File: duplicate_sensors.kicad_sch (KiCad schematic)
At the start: 0 parts

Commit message: IR + DC mic
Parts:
- added C1: 10nF, symbol Device:C
- added J1: SENO232_MIC, Connector_Audio:Jack_XLR_Neutrik_NC3FAAH_Horizontal, symbol Connector_Generic:Conn_01x03
- added Q1: AO3400A, Package_TO_SOT_SMD:SOT-23, symbol Transistor_FET:AO3400A
- added R1: 1k, symbol Device:R
- added R2: 39, Package_DIP:DIP-8_W7.62mm, symbol Device:R
- added R3: 100, Package_DIP:DIP-8_W7.62mm, symbol Device:R
- added R4: 100k, Package_DIP:DIP-8_W7.62mm, symbol Device:R
- added TSAL6200: LED, Package_DirectFET:DirectFET_MD, symbol Device:LED
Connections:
- new net: Q1.1 (G), R3.1, R4.1
- new net: J1.1 (Pin_1), R1.1
- new net: C1.1, R1.2
- new net: R2.2, TSAL6200.2 (A)
- new net: Q1.3 (D), TSAL6200.1 (K)
- new net +3.3V: J1.2 (Pin_2), R2.1
- new net GND: C1.2, J1.3 (Pin_3), Q1.2 (S), R4.2

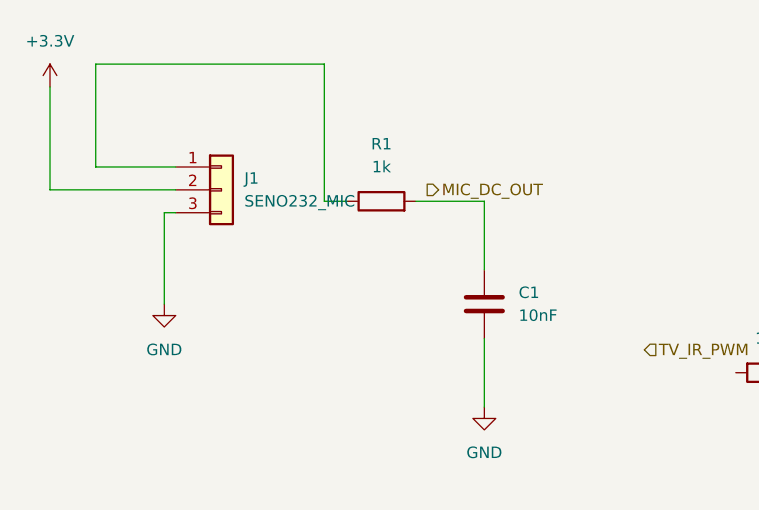
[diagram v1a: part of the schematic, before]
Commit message: Update duplicate_sensors.kicad_sch
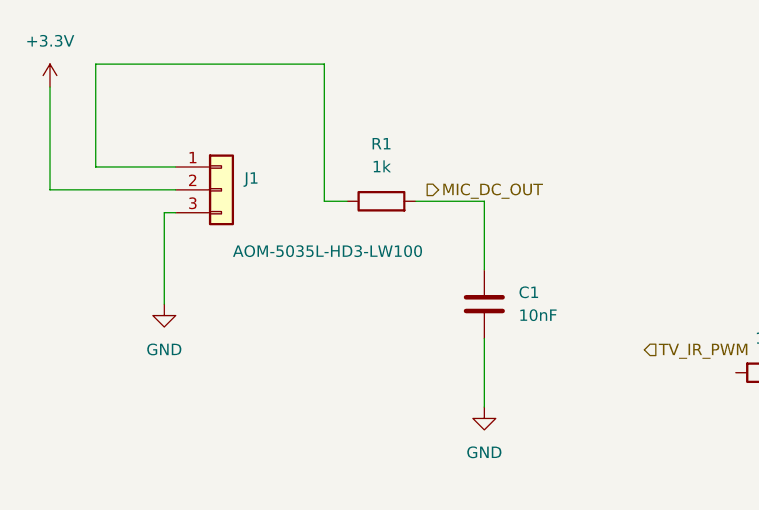
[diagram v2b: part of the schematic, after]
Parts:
- J1: value SENO232_MIC -> AOM-5035L-HD3-LW100
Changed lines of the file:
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@@
 		(in_pos_files yes)
 		(dnp no)
-		(fields_autoplaced yes)
 		(property "Reference" "J1"
 			(at 64.77 46.9899 0)
@@
 			)
 		)
-		(property "Value" "SENO232_MIC"
-			(at 64.77 49.5299 0)
+		(property "Value" "AOM-5035L-HD3-LW100"
+			(at 63.5 55.118 0)
 			(show_name no)
 			(do_not_autoplace no)

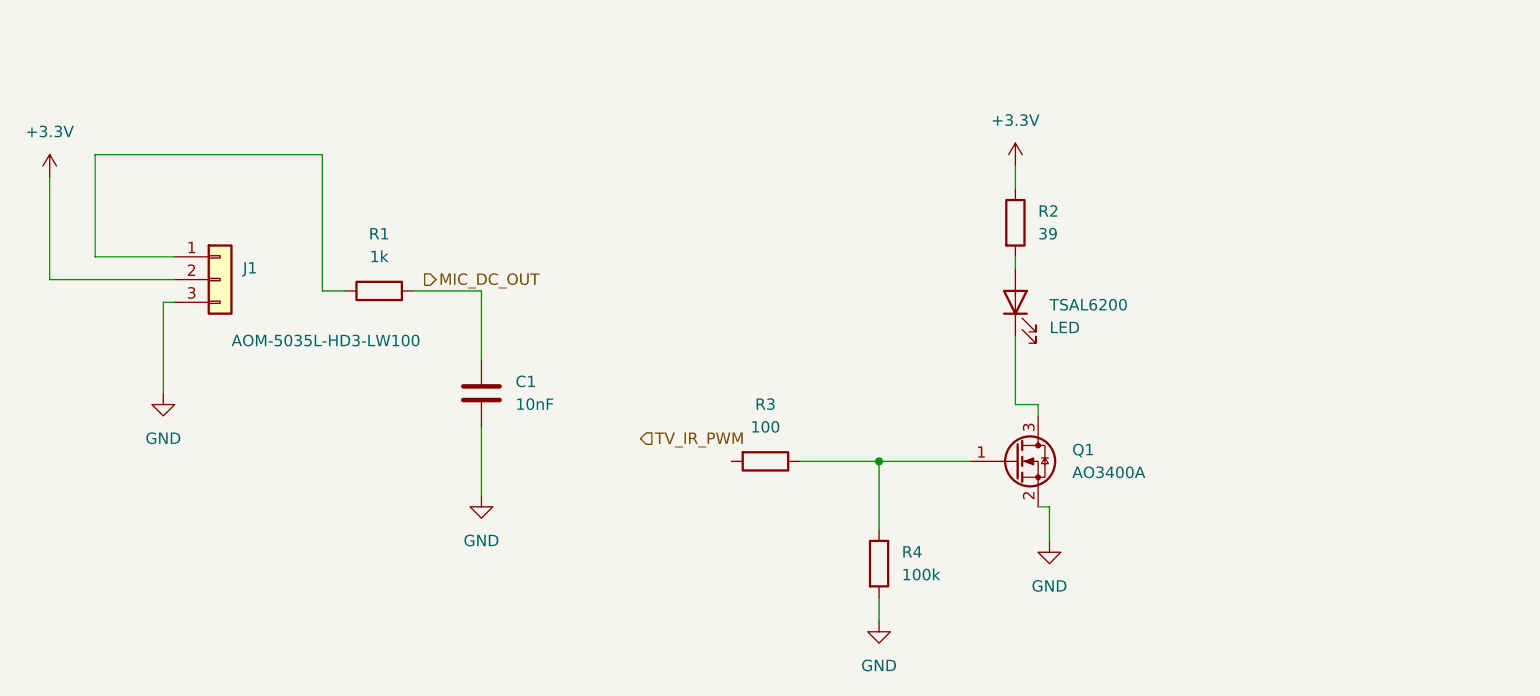
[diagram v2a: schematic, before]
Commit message: Update duplicate_sensors.kicad_sch
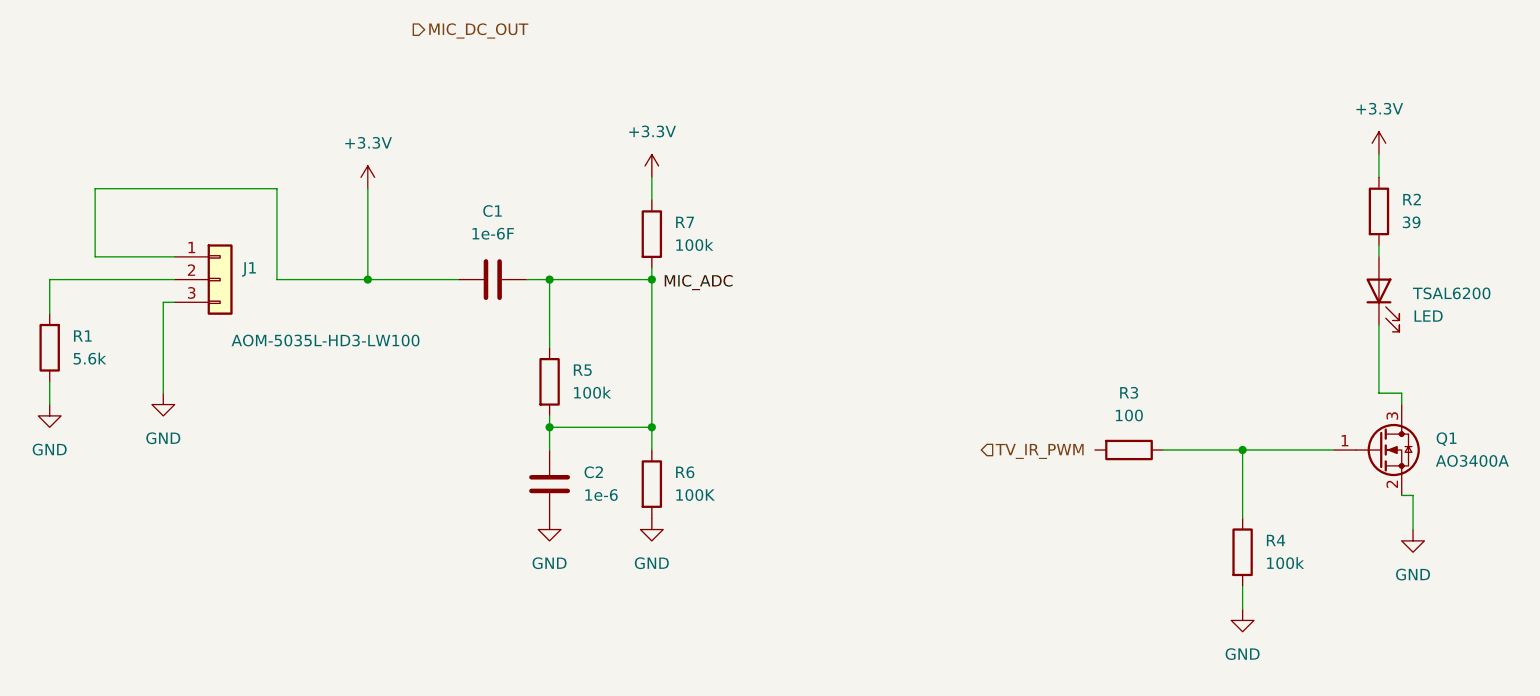
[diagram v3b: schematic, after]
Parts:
- added C2: 1e-6, symbol Device:C
- added R5, R7: 100k, Package_TO_SOT_SMD:SOT-23-5, symbol Device:R
- added R6: 100K, Package_TO_SOT_SMD:SOT-23-5, symbol Device:R
- C1: value 10nF -> 1e-6F
- R1: value 1k -> 5.6k
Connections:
- net +3.3V: now also C1.1, J1.1 (Pin_1), R7.1; no longer J1.2 (Pin_2)
- net GND: now also R1.1, C2.2, R6.2; no longer C1.2
- net at R1.2: now also J1.2 (Pin_2); no longer C1.1
- new net: C1.2, C2.1, R5.1, R5.2, R6.1, R7.2
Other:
- moved on the sheet: C1, Q1, R1, R2, R3, R4, TSAL6200
